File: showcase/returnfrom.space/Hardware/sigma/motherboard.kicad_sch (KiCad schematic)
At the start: 117 parts, among them J1 USB_C_Receptacle_USB2.0_16P, J19 Conn_01x08_Pin, J2 Conn_01x08_Socket, J26 Conn_01x02, J3 OLED, J4 Conn_02x03_Odd_Even, J5 Conn_02x04_Odd_Even, J6 Conn_02x03_Odd_Even, J7 Conn_01x02, Q3 BC817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

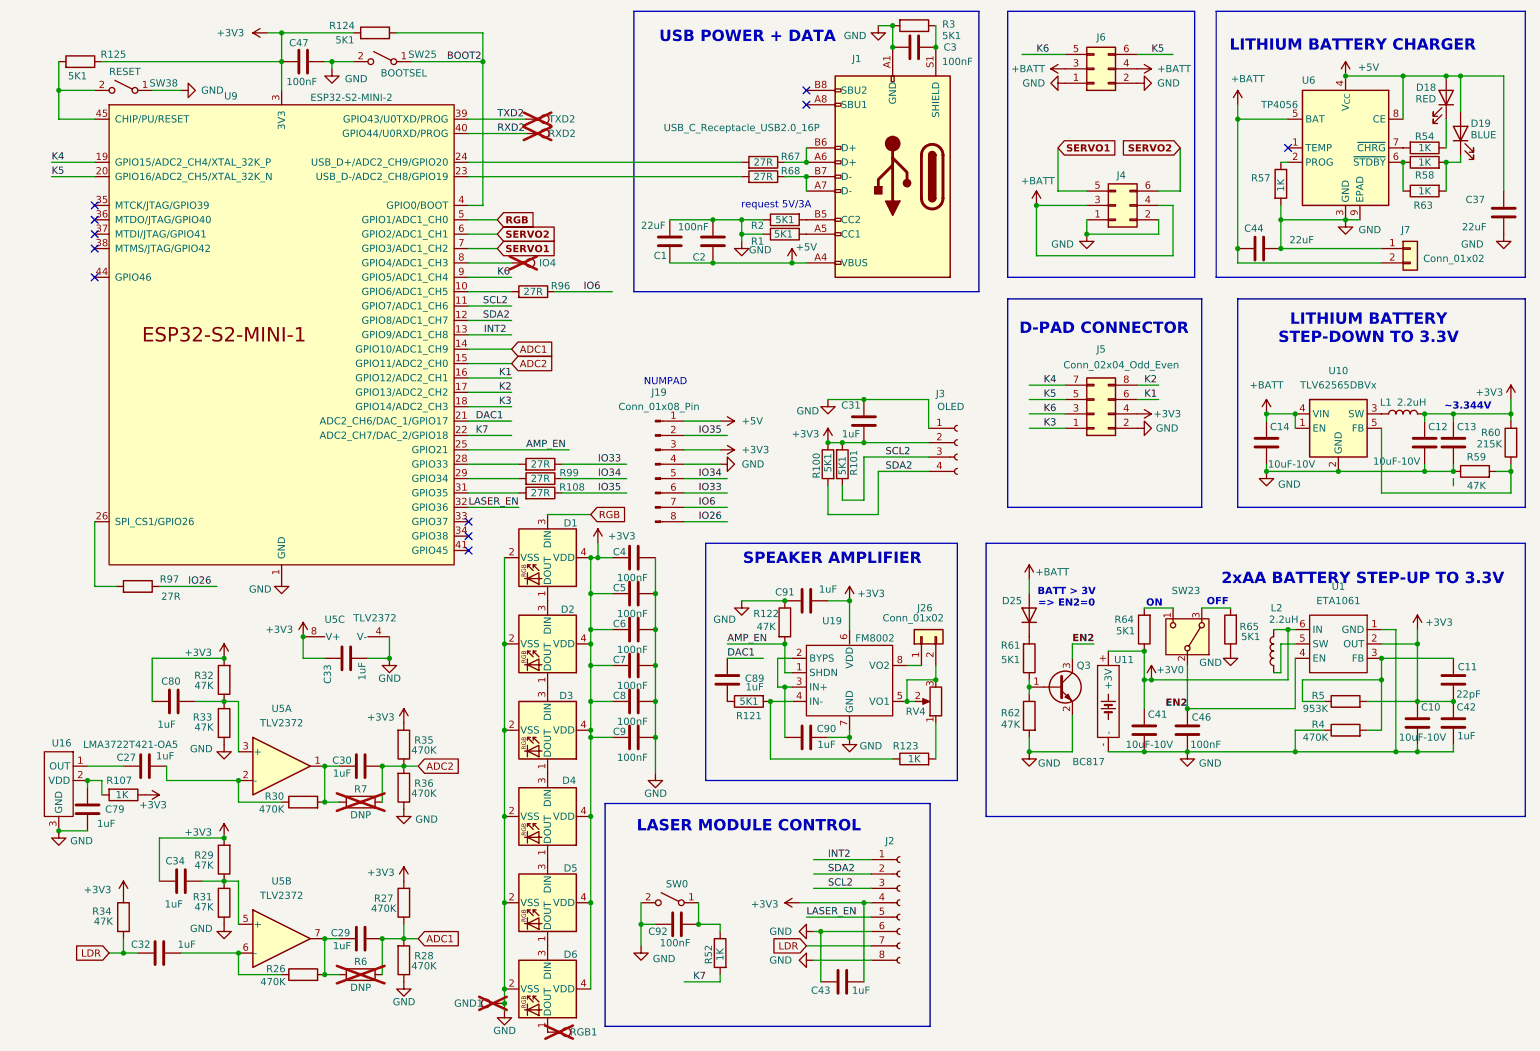
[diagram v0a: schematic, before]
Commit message: sigma fix - not validated
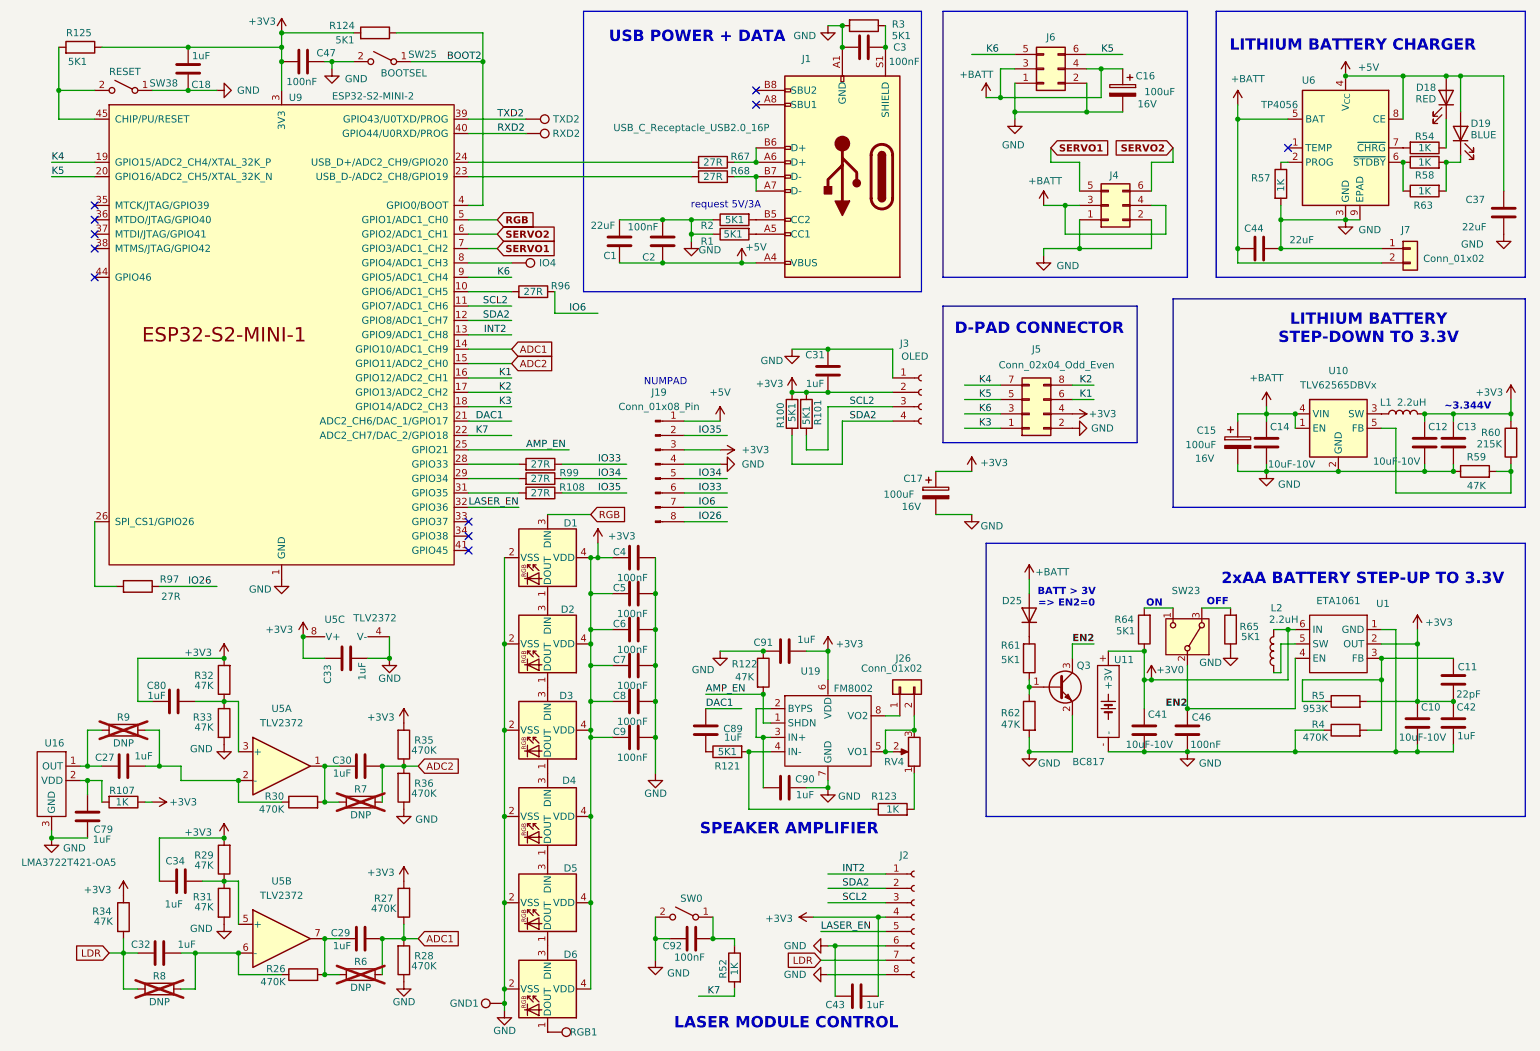
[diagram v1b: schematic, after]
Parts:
- added C15, C16, C17: 100uF, Capacitor_SMD:CP_Elec_6.3x5.4, symbol Device:C_Polarized
- added C18: 1uF, Capacitor_SMD:C_0402_1005Metric, symbol Device:C
- added R8, R9: DNP, Resistor_SMD:R_0402_1005Metric, symbol Device:R
- GND1, IO4, RGB1, RXD2, TXD2: now fitted
- J4, J6: footprint Connector_PinHeader_2.54mm:PinHeader_2x03_P2.54mm_Vertical -> Connector_PinHeader_2.54mm:PinHeader_2x03_P2.54mm_Horizontal
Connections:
- net +3V3: now also C17.1, C18.2
- net +BATT: now also C15.1, C16.1
- net GND: now also C15.2, C16.2, C17.2, C18.1
- net LDR: now also R8.1
- net at C27.1, U16.1 (OUT): now also R9.1
- net at C27.2, R30.1, U5.2 (-): now also R9.2
- net at C32.2, R26.1, U5.6 (-): now also R8.2
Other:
- moved on the sheet: C1, C2, C27, C3, C31, C43, C79, C89, C90, C91, C92, J1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
